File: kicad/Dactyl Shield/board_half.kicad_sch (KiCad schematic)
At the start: 31 parts, among them J301 JST, J302 Split, J303 Column, J304 Thumb, J305 External, J306 Row, J307 Display, J308 Vic, SW301 Battery, SW302 Reset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

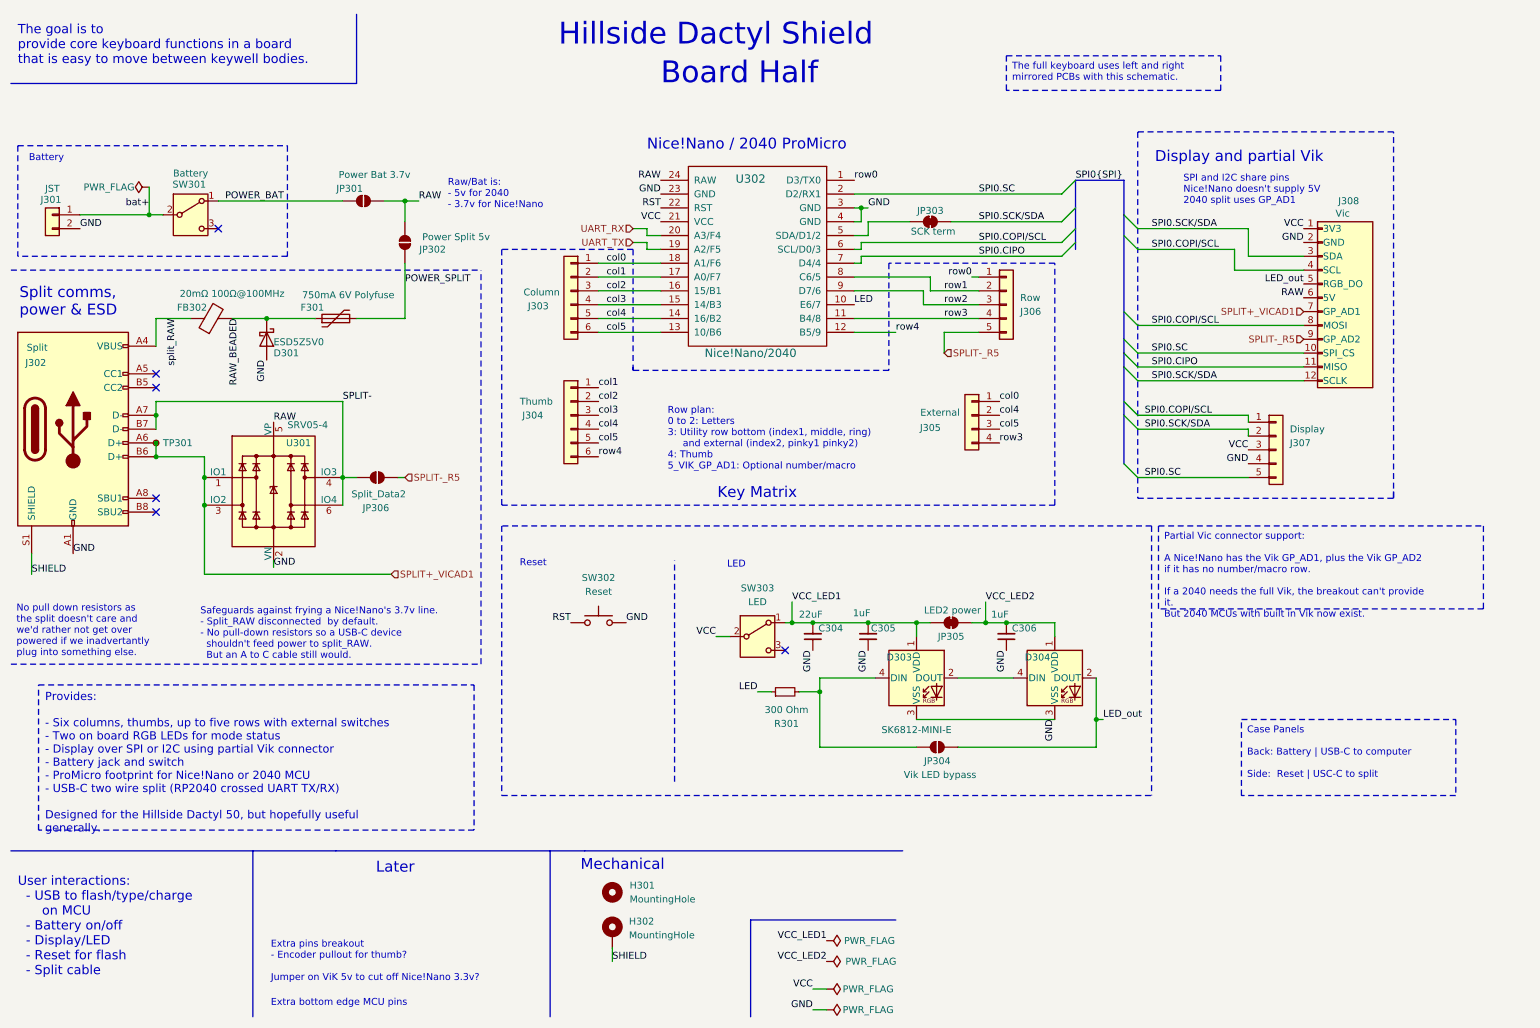
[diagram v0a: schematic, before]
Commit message: feat: usb shield to ground, jumper to case shield
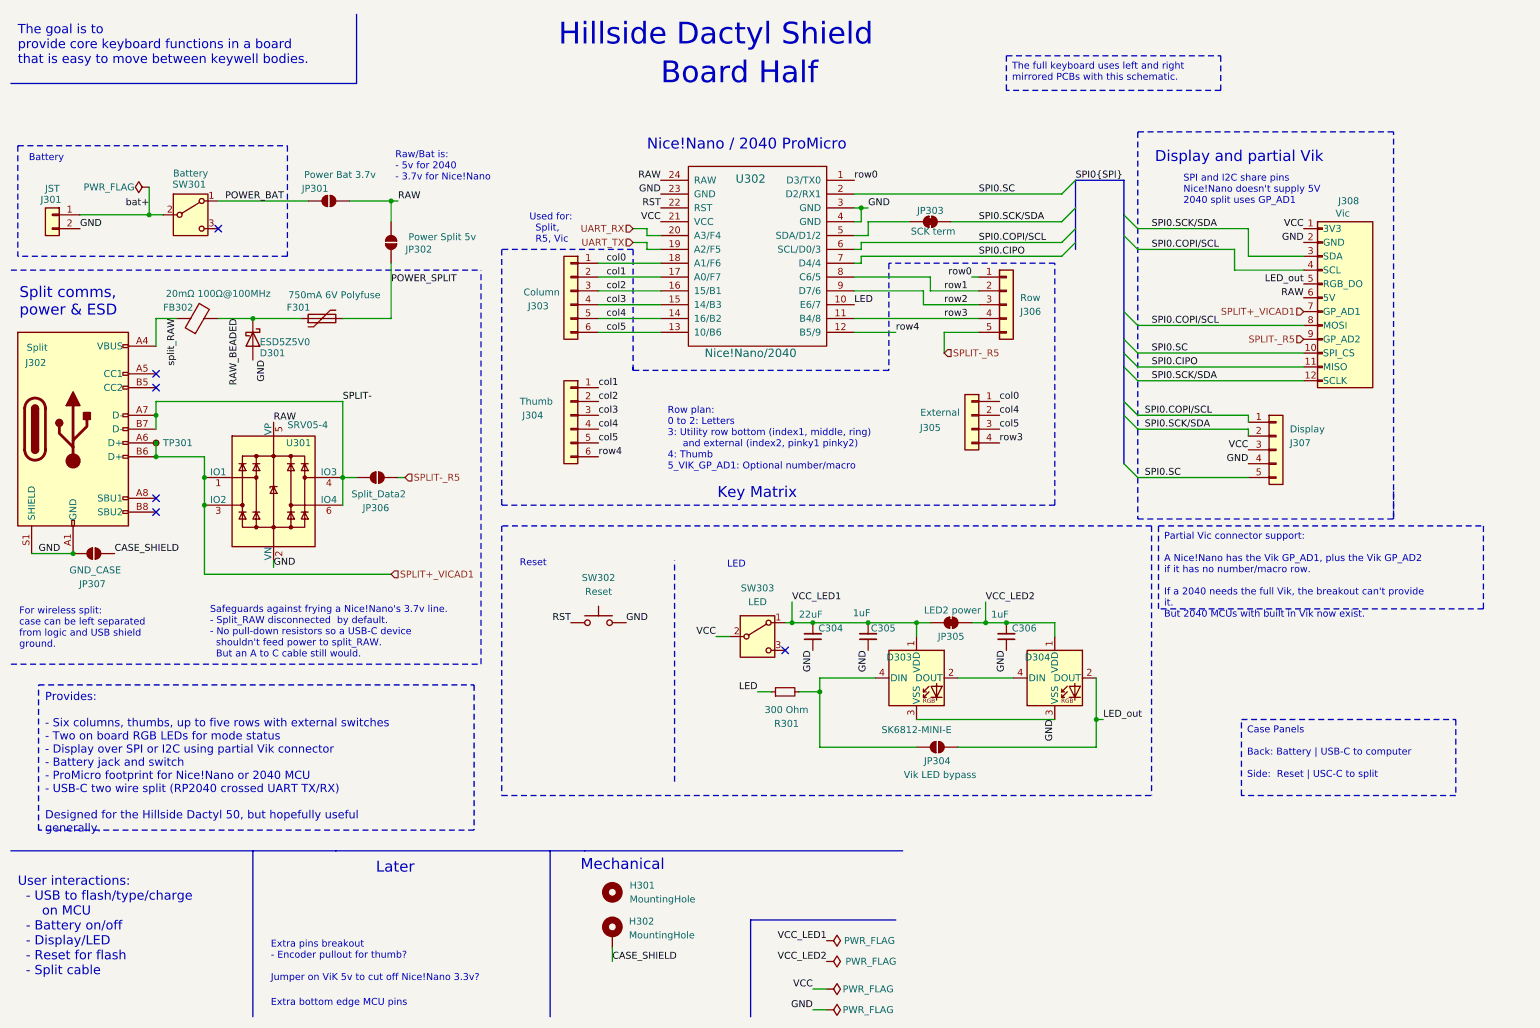
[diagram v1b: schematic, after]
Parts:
- added JP307: GND_CASE, Dactyl_basics:SolderJumper-2_P1.3mm_Open_RoundedPad1.0x1.5mm, symbol Jumper:SolderJumper_2_Open
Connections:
- net GND: now also J302.S1 (SHIELD), JP307.1 (A); no longer D301.2 (A)
- net SHIELD renamed CASE_SHIELD
- net CASE_SHIELD: now also JP307.2 (B); no longer J302.S1 (SHIELD)
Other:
- note added: "For wireless split: case can be left separated from logic and USB shield ground."
- note added: "Used for: Split, R5, Vic"
- note removed: "No pull down resistors as the split doesn't care and we'd rather not get over powered if we inadvertantly plug into something else."
- moved on the sheet: D301, F301, FB302, JP301, JP302

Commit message: feat: unchecked in changes, likely to LED
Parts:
- added D302: LED_Red, LED_THT:LED_D5.0mm, symbol Device:LED_Small
- added J309: ResA, Dactyl_basics:Conn_Pin_D0.8mm, symbol Connector:Conn_01x01_Socket
- added J312: ResB, Dactyl_basics:Conn_Pin_D0.8mm, symbol Connector:Conn_01x01_Socket
- added JP308: LED_Data, Jumper:SolderJumper-3_P1.3mm_Bridged12_RoundedPad1.0x1.5mm, symbol Jumper:Jumper_3_Bridged12
- added JP309: RGB, Dactyl_basics:SolderJumper-2_P1.3mm_Bridged_RoundedPad1.0x1.5mm, symbol Jumper:SolderJumper_2_Bridged
- added Q301: AO3400A, Package_TO_SOT_SMD:SOT-23, symbol Transistor_FET:AO3400A
- added R302, R305, R306: 33, Resistor_SMD:R_0805_2012Metric_Pad1.20x1.40mm_HandSolder, symbol Device:R_Small
- added R303: 300, Resistor_SMD:R_0603_1608Metric, symbol Device:R_Small
- added R304: 10k, Resistor_SMD:R_0603_1608Metric, symbol Device:R_Small
- C304, C305, C306: Role Power delivery -> Power
- H301, H302: Role (none) -> Case
- J303, J304, J305, J306: Role (none) -> Matrix
- J307, JP303: Role (none) -> Display
- JP301, JP302: Role (none) -> Power
- JP304: value Vik LED bypass -> Vik bypass; Role (none) -> LED
- JP305: value LED2 power -> RGB2; Role (none) -> LED
- JP306: Role (none) -> Split
- JP307: footprint Dactyl_basics:SolderJumper-2_P1.3mm_Open_RoundedPad1.0x1.5mm -> Dactyl_basics:SolderJumper-2_P1.3mm_Bridged_RoundedPad1.0x1.5mm; symbol Jumper:SolderJumper_2_Open -> Jumper:SolderJumper_2_Bridged; Role (none) -> Case
- R301: value 300 Ohm -> 300
- TP301: Config (none) -> DNF; Role (none) -> Split
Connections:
- net GND: now also D301.2 (A), Q301.2 (S), R304.1
- net LED: now also JP308.2 (C); no longer R301.1
- net VCC_LED1: now also D302.1 (K), J309.1 (Pin_1), R302.2; no longer C304.2, C305.2, D303.1 (VDD), JP305.1 (A), SW303.1 (A)
- net VCC_LED2: now also R302.1, R305.2; no longer C306.2, D304.1 (VDD), JP305.2 (B)
- new net: JP308.1 (A), R303.1, R304.2
- new net: Q301.1 (G), R303.2
- new net: JP308.3 (B), R301.1
- new net VCC_LED: C304.2, D302.2 (A), JP309.1 (A), SW303.1 (A)
- new net VCC_LED3: R305.1, R306.2
- new net VCC_LED4: J312.1 (Pin_1), Q301.3 (D), R306.1
- new net VCC_RGB1: C305.2, D303.1 (VDD), JP305.1 (A), JP309.2 (B)
- new net VCC_RGB2: C306.2, D304.1 (VDD), JP305.2 (B)
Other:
- note added: "Bare one color"
- note added: "Power"
- note added: "Smart RGB"
- note added: "Through hole resistor option"
- note added: "or"
- moved on the sheet: C304, C305, C306, D303, D304, J303, J304, J305, J306, JP301, JP302, JP303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

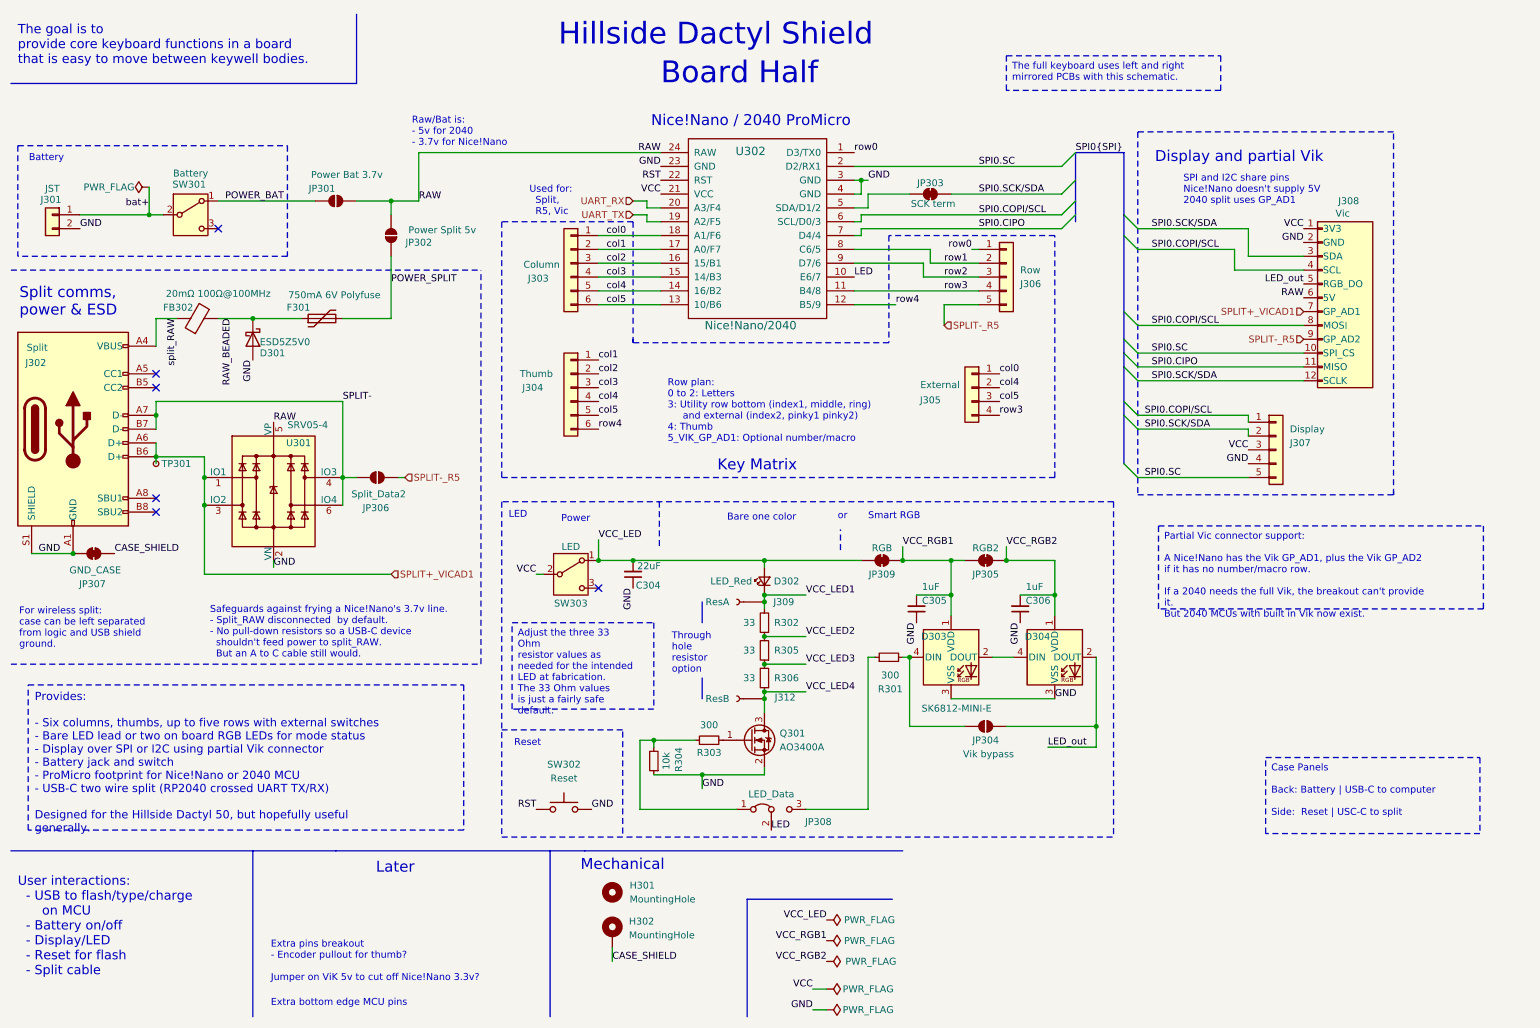
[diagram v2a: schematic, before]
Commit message: feat: route ground traces, fix mirror positions
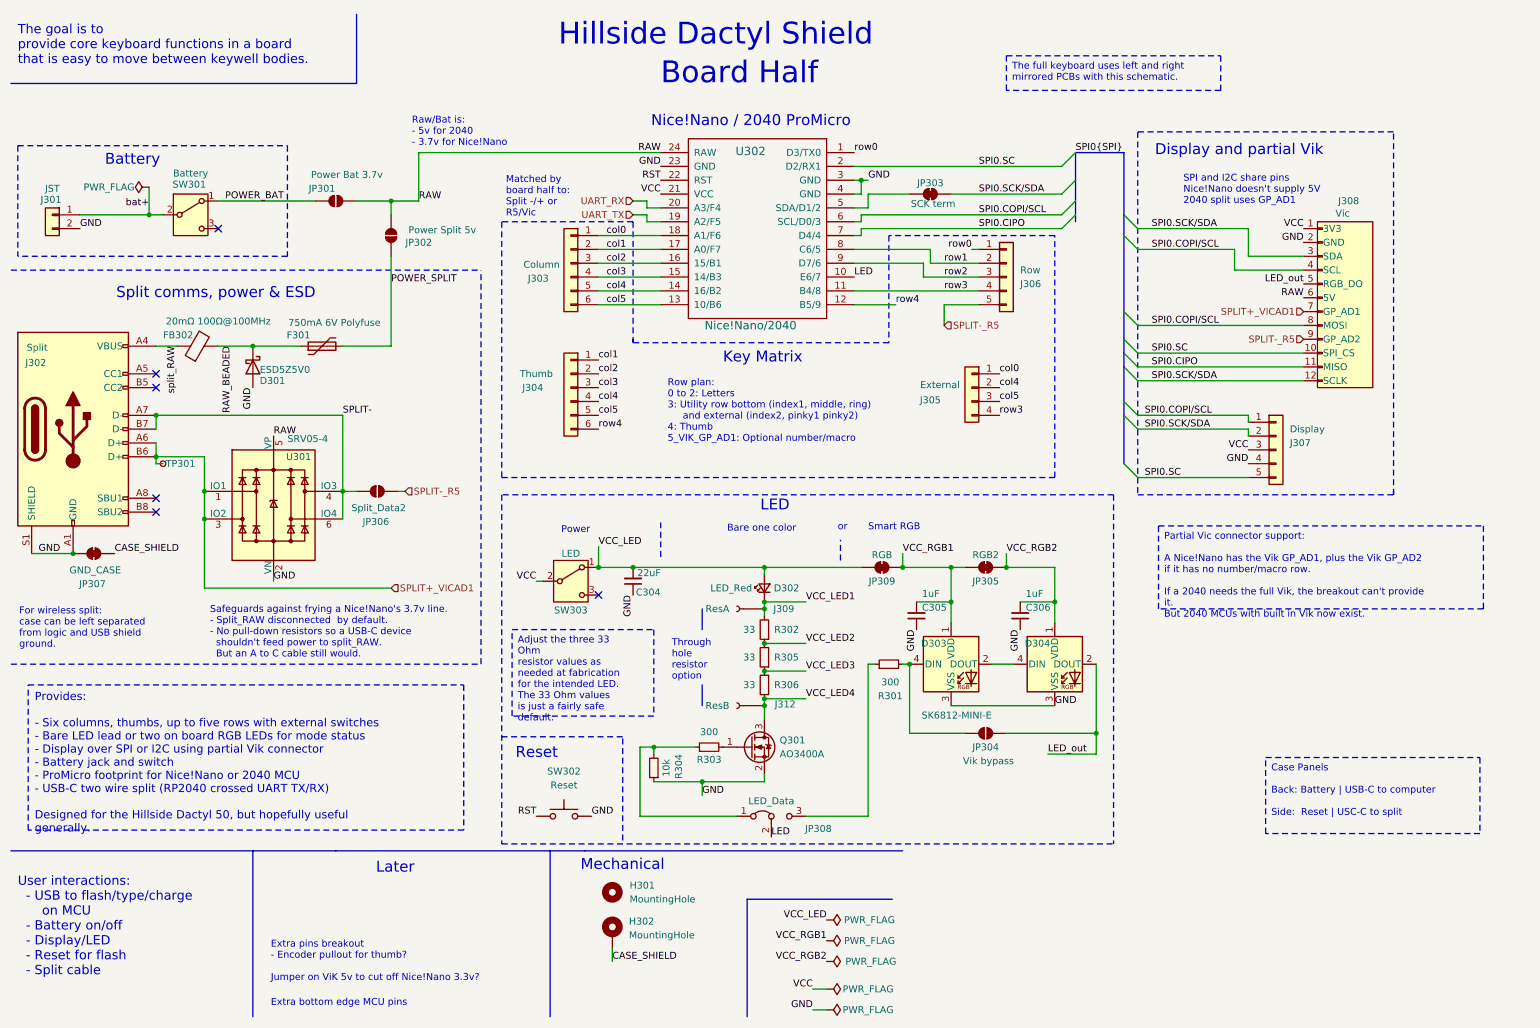
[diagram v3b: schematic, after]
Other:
- note added: "Matched by board half to: Split -/+ or R5/Vic"
- note removed: "Used for: Split, R5, Vic"
- moved on the sheet: C304, C305, C306, D301, D302, D303, D304, F301, FB302, J309, J312, JP304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
